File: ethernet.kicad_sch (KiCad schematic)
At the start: 62 parts, among them J6 Bus_RJ45_5-2337992-8, U15 KSZ9031RNXCA, Y2 Resonator_25MHz_ABM8G

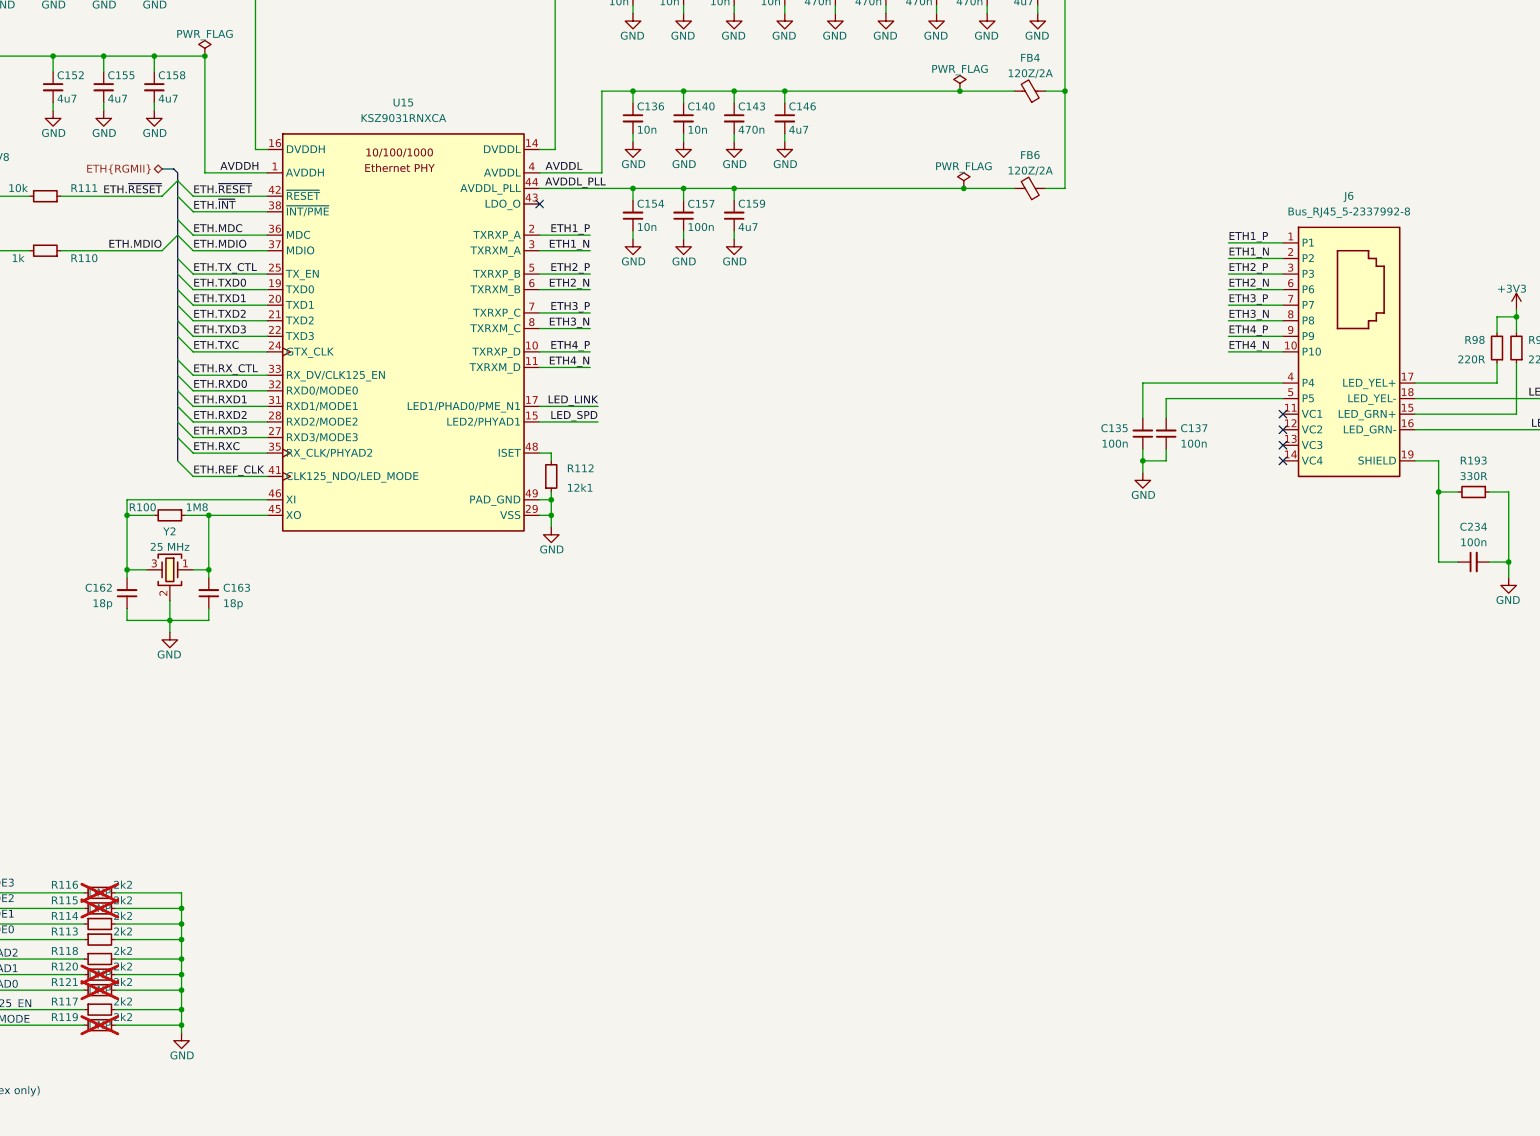
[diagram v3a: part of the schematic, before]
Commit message: [#67725] Update ethernet
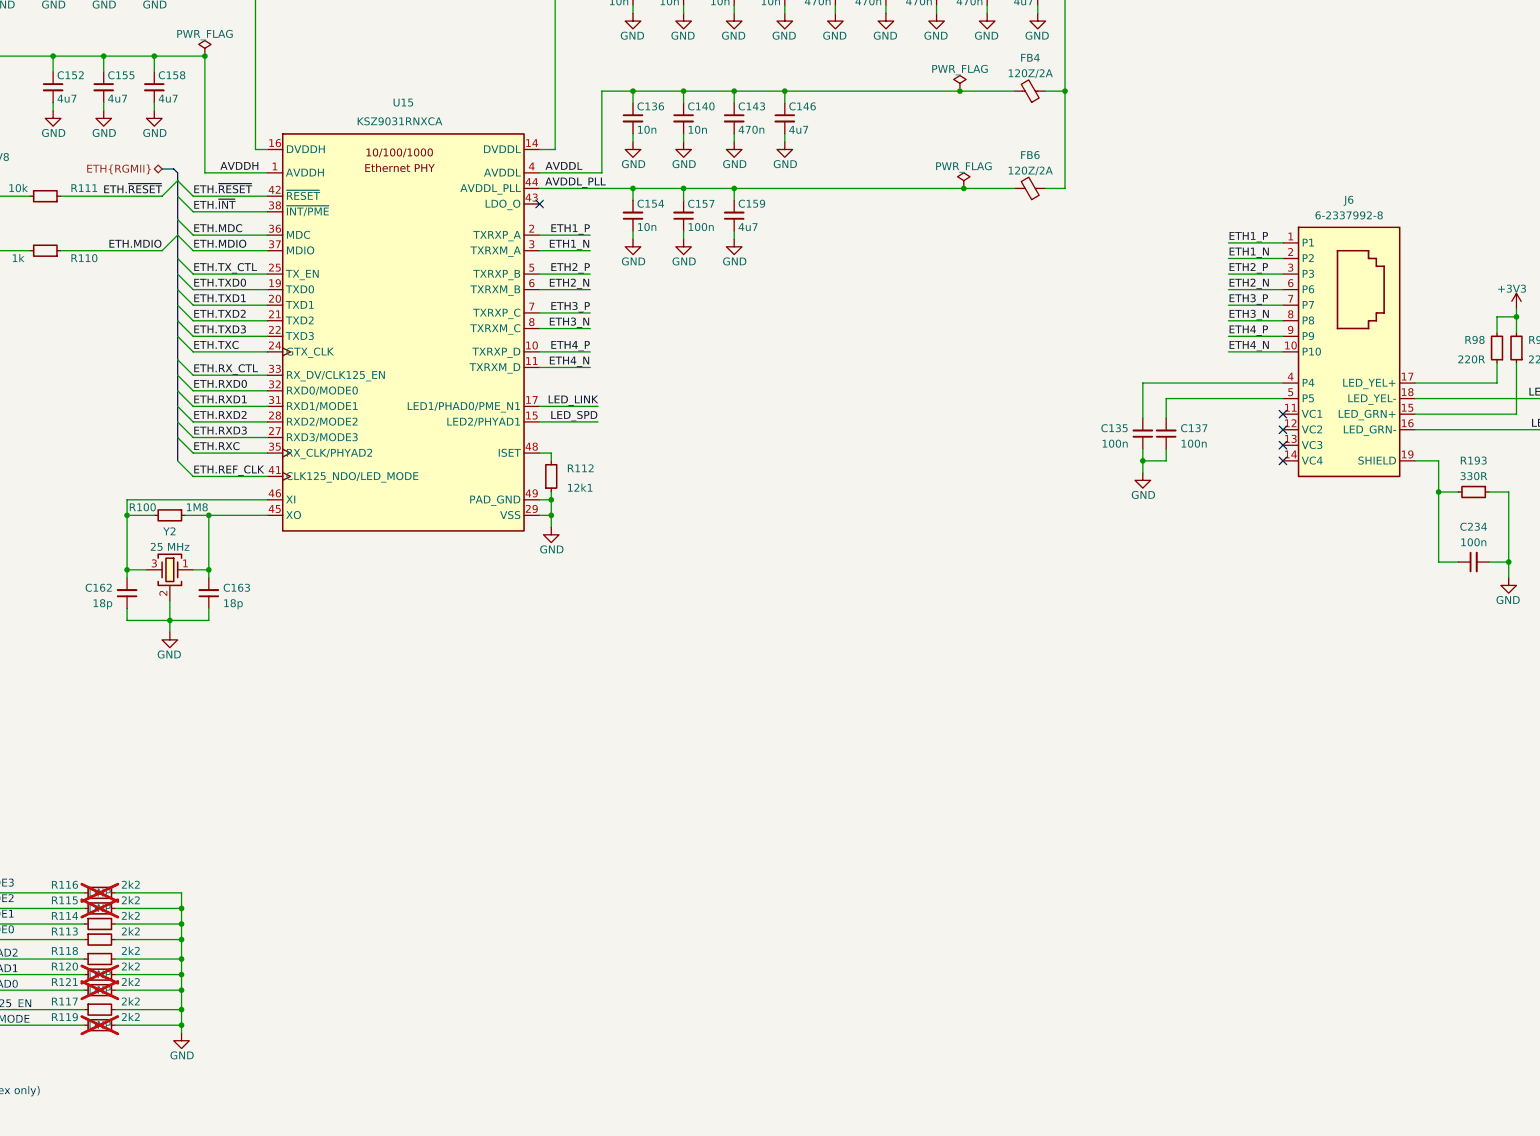
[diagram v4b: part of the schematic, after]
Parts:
- removed J6: Bus_RJ45_5-2337992-8, antmicro-footprints:RJ45_X-2337992-8_Horizontal, symbol antmicroModularConnectorsJacksWithMagnetics:Bus_RJ45_5-2337992-8
- added J6: Bus_RJ45_6-2337992-8, antmicro-footprints:RJ45_X-2337992-8_Horizontal, symbol antmicroModularConnectorsJacksWithMagnetics:Bus_RJ45_6-2337992-8
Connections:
- net ETH1_N: now also J6.2 (P2)
- net ETH1_P: now also J6.1 (P1)
- net ETH2_N: now also J6.6 (P6)
- net ETH2_P: now also J6.3 (P3)
- net ETH3_N: now also J6.8 (P8)
- net ETH3_P: now also J6.7 (P7)
- net ETH4_N: now also J6.10 (P10)
- net ETH4_P: now also J6.9 (P9)
- net LED_LINK: now also J6.18 (LED_YEL-)
- net LED_SPD: now also J6.16 (LED_GRN-)
- net at R98.1: now also J6.17 (LED_YEL+)
- net at R99.1: now also J6.15 (LED_GRN+)
- net at C135.2: now also J6.4 (P4)
- net at C137.2: now also J6.5 (P5)
- net at C234.1, R193.2: now also J6.19 (SHIELD), J6.20 (SHIELD)
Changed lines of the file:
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@@
   )
   (symbol (lib_id "antmicroInterfaceControllers:KSZ9031RNXCA") (at 130.81 85.09 0) (unit 1)
-    (in_bom yes) (on_board yes) (dnp no) (fields_autoplaced)
+    (in_bom yes) (on_board yes) (dnp no)
     (property "Reference" "U15" (at 153.035 77.47 0)
       (effects (font (size 1.27 1.27)))
     )
     (property "Value" "KSZ9031RNXCA" (at 153.035 80.01 0)
-      (effects (font (size 1.27 1.27) (thickness 0.15)))
+      (effects (font (size 1.27 1.27) (thickness 0.15)) hide)
     )
     (property "Footprint" "antmicro-footprints:QFN-48-1EP_7x7x0.9mm_P0.5mm_EP3.5x3.5mm" (at 207.01 95.25 0)
@@
       (effects (font (size 1.27 1.27) (thickness 0.15)) (justify left bottom) hide)
     )
-    (property "MPN" "KSZ9031RNXCA" (at 207.01 102.87 0)
-      (effects (font (size 1.27 1.27) (thickness 0.15)) (justify left bottom) hide)
+    (property "MPN" "KSZ9031RNXCA" (at 145.415 81.28 0)
+      (effects (font (size 1.27 1.27) (thickness 0.15)) (justify left bottom))
     )
     (property "Author" "Antmicro" (at 207.01 105.41 0)
@@
       (effects (font (size 1.27 1.27) (thickness 0.15)) (justify left bottom) hide)
     )
-    (property "Val" "2k2" (at 107.315 212.725 0)
+    (property "Val" "2k2" (at 108.585 212.725 0)
       (effects (font (size 1.27 1.27) (thickness 0.15)))
     )
@@
       (effects (font (size 1.27 1.27) (thickness 0.15)) (justify left bottom) hide)
     )
-    (property "Val" "2k2" (at 107.315 210.185 0)
+    (property "Val" "2k2" (at 108.585 210.185 0)
       (effects (font (size 1.27 1.27) (thickness 0.15)))
     )
@@
       (effects (font (size 1.27 1.27) (thickness 0.15)) (justify left bottom) hide)
     )
-    (property "Val" "2k2" (at 107.315 207.645 0)
+    (property "Val" "2k2" (at 108.585 207.645 0)
       (effects (font (size 1.27 1.27) (thickness 0.15)))
     )
@@
       (effects (font (size 1.27 1.27) (thickness 0.15)) (justify left bottom) hide)
     )
-    (property "Val" "2k2" (at 107.315 205.105 0)
+    (property "Val" "2k2" (at 108.585 205.105 0)
       (effects (font (size 1.27 1.27) (thickness 0.15)))
     )
@@
       (effects (font (size 1.27 1.27) (thickness 0.15)) (justify left bottom) hide)
     )
-    (property "Val" "2k2" (at 107.315 224.155 0)
+    (property "Val" "2k2" (at 108.585 224.155 0)
       (effects (font (size 1.27 1.27) (thickness 0.15)))
     )
@@
       (effects (font (size 1.27 1.27) (thickness 0.15)) (justify left bottom) hide)
     )
-    (property "Val" "2k2" (at 107.315 215.9 0)
+    (property "Val" "2k2" (at 108.585 215.9 0)
       (effects (font (size 1.27 1.27) (thickness 0.15)))
     )
@@
       (effects (font (size 1.27 1.27) (thickness 0.15)) (justify left bottom) hide)
     )
-    (property "Val" "2k2" (at 107.315 218.44 0)
+    (property "Val" "2k2" (at 108.585 218.44 0)
       (effects (font (size 1.27 1.27) (thickness 0.15)))
     )
@@
       (effects (font (size 1.27 1.27) (thickness 0.15)) (justify left bottom) hide)
     )
-    (property "Val" "2k2" (at 107.315 220.98 0)
+    (property "Val" "2k2" (at 108.585 220.98 0)
       (effects (font (size 1.27 1.27) (thickness 0.15)))
     )
@@
       (effects (font (size 1.27 1.27) (thickness 0.15)) (justify left bottom) hide)
     )
-    (property "Val" "2k2" (at 107.315 226.695 0)
+    (property "Val" "2k2" (at 108.585 226.695 0)
       (effects (font (size 1.27 1.27) (thickness 0.15)))
     )
@@
     )
   )
+  (symbol (lib_id "antmicroModularConnectorsJacksWithMagnetics:Bus_RJ45_6-2337992-8") (at 296.545 100.33 0) (unit 1)
+    (in_bom yes) (on_board yes) (dnp no) (fields_autoplaced)
+    (property "Reference" "J6" (at 307.34 93.345 0)
+      (effects (font (size 1.27 1.27) (thickness 0.15)))
+    )
+    (property "Value" "Bus_RJ45_6-2337992-8" (at 332.105 107.95 0)
+      (effects (font (size 1.27 1.27) (thickness 0.15)) (justify left bottom) hide)
+    )
+    (property "Footprint" "antmicro-footprints:RJ45_X-2337992-8_Horizontal" (at 332.105 110.49 0)
+      (effects (font (size 1.27 1.27) (thickness 0.15)) (justify left bottom) hide)
+    )
+    (property "Datasheet" "https://www.te.com/commerce/DocumentDelivery/DDEController?Action=showdoc&DocId=Customer+Drawing%7F6-2337992-8%7FA1%7Fpdf%7FEnglish%7FENG_CD_6-2337992-8_A1.pdf%7F6-2337992-8" (at 332.105 113.03 0)
+      (effects (font (size 1.27 1.27) (thickness 0.15)) (justify left bottom) hide)
+    )
+    (property "MPN" "6-2337992-8" (at 307.34 95.885 0)
+      (effects (font (size 1.27 1.27) (thickness 0.15)))
+    )
+    (property "Manufacturer" "TE Connectivity" (at 332.105 115.57 0)
+      (effects (font (size 1.27 1.27) (thickness 0.15)) (justify left bottom) hide)
+    )
+    (property "Author" "Antmicro" (at 332.105 118.11 0)
+      (effects (font (size 1.27 1.27) (thickness 0.15)) (justify left bottom) hide)
+    )
+    (property "License" "Apache-2.0" (at 332.105 120.65 0)
+      (effects (font (size 1.27 1.27) (thickness 0.15)) (justify left bottom) hide)
+    )
+    (pin "4")
+    (pin "7")
+    (pin "8")
+    (pin "6")
+    (pin "9")
+    (pin "17")
+    (pin "16")
+    (pin "13")
+    (pin "12")
+    (pin "14")
+    (pin "11")
+    (pin "3")
+    (pin "19")
+    (pin "15")
+    (pin "2")
+    (pin "20")
+    (pin "5")
+    (pin "18")
+    (pin "10")
+    (pin "1")
+    (instances
+      (project "data-center-rdimm-ddr5-tester"
+        (path "/1faa6543-e26a-4449-8bac-ee14b9f19e5f/00000000-0000-0000-0000-00005f982999"
+          (reference "J6") (unit 1)
+        )
+      )
+    )
+  )
   (symbol (lib_id "antmicropower:+1V2") (at 260.985 52.07 0) (mirror y) (unit 1)
     (in_bom yes) (on_board yes) (dnp no) (fields_autoplaced)
@@
         )
       )
-    )
-  )
-  (symbol (lib_name "Bus_RJ45_5-2337992-8_1") (lib_id "antmicroModularConnectorsJacksWithMagnetics:Bus_RJ45_5-2337992-8") (at 296.545 100.33 0) (unit 1)
-    (in_bom yes) (on_board yes) (dnp no) (fields_autoplaced)
-    (property "Reference" "J6" (at 307.34 92.71 0)
-      (effects (font (size 1.27 1.27) (thickness 0.15)))
-    )
-    (property "Value" "Bus_RJ45_5-2337992-8" (at 307.34 95.25 0)
-      (effects (font (size 1.27 1.27) (thickness 0.15)))
-    )
-    (property "Footprint" "antmicro-footprints:RJ45_X-2337992-8_Horizontal" (at 332.105 107.95 0)
-      (effects (font (size 1.27 1.27) (thickness 0.15)) (justify left bottom) hide)
-    )
-    (property "Datasheet" "https://www.te.com/commerce/DocumentDelivery/DDEController?Action=showdoc&DocId=Customer+Drawing%7F5-2337992-8%7FA%7Fpdf%7FEnglish%7FENG_CD_5-2337992-8_A.pdf%7F5-2337992-8" (at 332.105 110.49 0)
-      (effects (font (size 1.27 1.27) (thickness 0.15)) (justify left bottom) hide)
-    )
-    (property "MPN" "5-2337992-8" (at 332.105 113.03 0)
-      (effects (font (size 1.27 1.27) (thickness 0.15)) (justify left bottom) hide)
-    )
-    (property "Manufacturer" "TE Connectivity" (at 332.105 115.57 0)
-      (effects (font (size 1.27 1.27) (thickness 0.15)) (justify left bottom) hide)
-    )
-    (property "Author" "Antmicro" (at 332.105 118.11 0)
-      (effects (font (size 1.27 1.27) (thickness 0.15)) (justify left bottom) hide)
-    )
-    (property "License" "Apache-2.0" (at 332.105 120.65 0)
-      (effects (font (size 1.27 1.27) (thickness 0.15)) (justify left bottom) hide)
-    )
-    (property "VSD_Class" "Ethernet" (at 332.105 123.19 0)
-      (effects (font (size 1.27 1.27)) (justify left bottom) hide)
-    )
-    (pin "6")
-    (pin "7")
-    (pin "5")
-    (pin "9")
-    (pin "8")
-    (pin "11")
-    (pin "2")
-    (pin "12")
-    (pin "18")
-    (pin "17")
-    (pin "19")
-    (pin "4")
-    (pin "16")
-    (pin "20")
-    (pin "3")
-    (pin "13")
-    (pin "14")
-    (pin "1")
-    (pin "10")
-    (pin "15")
-    (instances
-      (project "data-center-rdimm-ddr5-tester"
-        (path "/1faa6543-e26a-4449-8bac-ee14b9f19e5f/00000000-0000-0000-0000-00005f982999"
-          (reference "J6") (unit 1)
-        )
-      )

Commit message: [#68016] Clean-up the schematic
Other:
- note added: "Ethernet PHY"
- note added: "RJ45 connector"
- moved on the sheet: C134, C135, C136, C137, C138, C139, C140, C141, C142, C143, C144, C145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

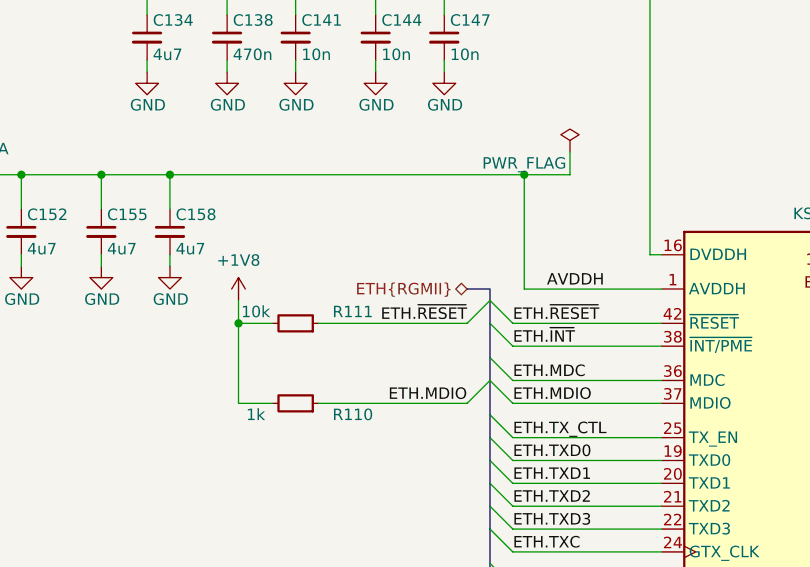
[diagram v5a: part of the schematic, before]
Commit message: [#68016] Improve bus entry marking
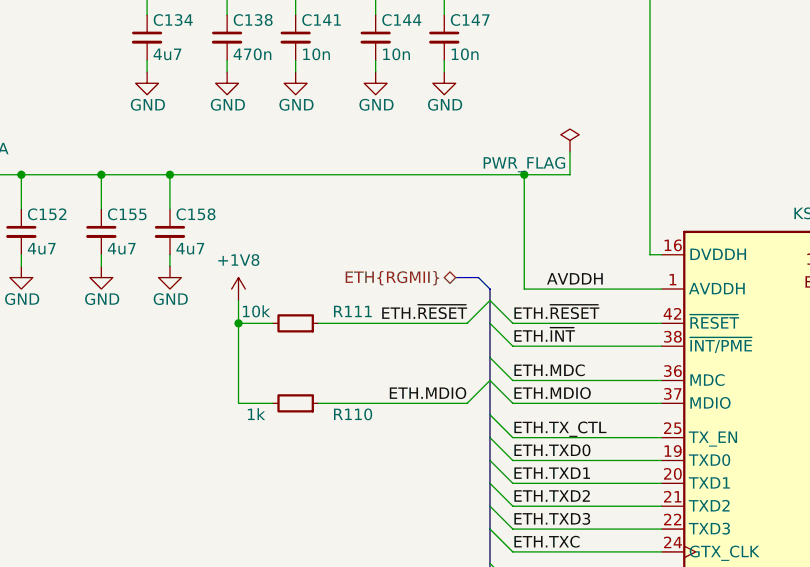
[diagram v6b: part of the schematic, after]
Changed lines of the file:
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@@
     (stroke (width 0) (type default))
   )
+  (bus (pts (xy 88.9 135.89) (xy 90.17 137.16))
+    (stroke (width 0) (type default))
+  )
   (wire (pts (xy 317.5 180.34) (xy 356.87 180.34))
     (stroke (width 0) (type default))
@@
     (stroke (width 0) (type default))
   )
-  (bus (pts (xy 87.63 137.16) (xy 90.17 137.16))
+  (bus (pts (xy 86.36 135.89) (xy 88.9 135.89))
     (stroke (width 0) (type default))
   )
@@
     (effects (font (size 1.27 1.27)) (justify right bottom))
   )
-  (hierarchical_label "ETH{RGMII}" (shape bidirectional) (at 87.63 137.16 180) (fields_autoplaced)
+  (hierarchical_label "ETH{RGMII}" (shape bidirectional) (at 86.36 135.89 180) (fields_autoplaced)
     (effects (font (size 1.27 1.27)) (justify right))
   )

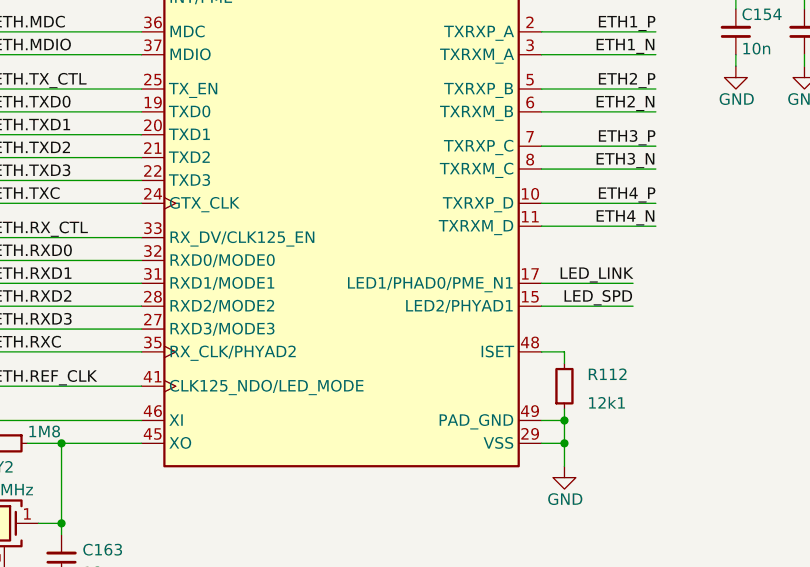
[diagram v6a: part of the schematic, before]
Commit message: [#68016] Solve ERC warrings and errors
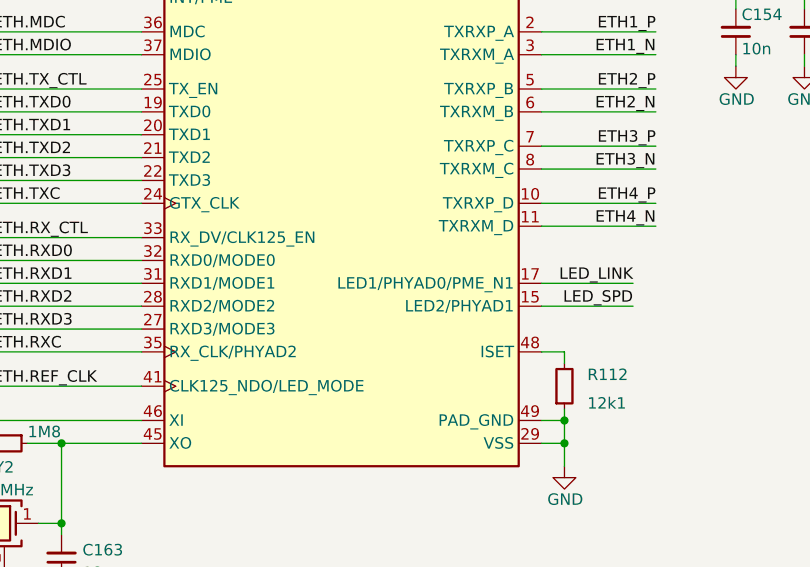
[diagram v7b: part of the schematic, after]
